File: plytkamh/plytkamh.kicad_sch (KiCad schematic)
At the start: 50 parts, among them J1 USB_C_Receptacle_USB2.0_16P, J2 BOOT0, J3 Conn_01x06, Q1 TEMT6000X01, SW1 RESET, SW2 USER, U1 USBLC6-2SC6, U2 LDL1117S33R, U3 STM32F446RETx, U4 BME280, Y1 12MHz

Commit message: Assign footprints
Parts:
- added J4: COMM, Connector_PinHeader_2.54mm:PinHeader_2x10_P2.54mm_Vertical, symbol Connector_Generic:Conn_02x10_Odd_Even
- added J5: ANALOG_GPIO, Connector_PinHeader_2.54mm:PinHeader_2x10_P2.54mm_Vertical, symbol Connector_Generic:Conn_02x10_Odd_Even
- C1, C10, C11, C12, C13, C14, C15, C16, C17, C18, C2, C3, C4, C5, C6, C7, C8, C9: footprint (none) -> Capacitor_SMD:C_0603_1608Metric
- D2, D3, D4, D5, D6: footprint (none) -> LED_SMD:LED_0603_1608Metric
- F1: footprint (none) -> Fuse:Fuse_1812_4532Metric
- FB1: footprint (none) -> Inductor_SMD:L_0603_1608Metric
- J1: footprint (none) -> Connector_USB:USB_C_Receptacle_GCT_USB4105-xx-A_16P_TopMnt_Horizontal
- J2: footprint (none) -> Connector_PinHeader_2.54mm:PinHeader_1x02_P2.54mm_Vertical
- J3: footprint (none) -> Connector_PinHeader_2.54mm:PinHeader_1x06_P2.54mm_Vertical
- R1, R10, R11, R12, R13, R2, R3, R4, R5, R6, R7, R8, R9: footprint (none) -> Resistor_SMD:R_0603_1608Metric
- SW1, SW2: footprint (none) -> Button_Switch_THT:SW_PUSH_6mm
- U2: footprint LDL1117S33R:SOT230P700X180-4N -> Package_TO_SOT_SMD:SOT-223
- Y1: footprint (none) -> Crystal:Crystal_SMD_3225-4Pin_3.2x2.5mm
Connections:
- net +3.3V: now also J4.1 (Pin_1), J5.1 (Pin_1)
- net +5V: now also J4.2 (Pin_2)
- net GND: now also J4.20 (Pin_20), J4.3 (Pin_3), J4.4 (Pin_4), J5.2 (Pin_2), J5.20 (Pin_20)
- net I2C1_SCL: now also J4.9 (Pin_9)
- net I2C1_SDA: now also J4.10 (Pin_10)
- net PA1: now reaches U3.15 (PA1)
- net PA1: now also J5.9 (Pin_9)
- net USART2_TX: now reaches U3.16 (PA2)
- net USART2_TX: now also J4.5 (Pin_5)
- net USART2_RX: now reaches U3.17 (PA3)
- net USART2_RX: now also J4.6 (Pin_6)
- net PA4: now reaches U3.20 (PA4)
- net PA4: now also J5.10 (Pin_10)
- net PA6: now reaches U3.22 (PA6)
- net PA6: now also J5.13 (Pin_13)
- net PA7: now reaches U3.23 (PA7)
- net PA7: now also J5.14 (Pin_14)
- net PC4: now reaches U3.24 (PC4)
- net PC4: now also J5.7 (Pin_7)
- net PC5: now reaches U3.25 (PC5)
- net PC5: now also J5.8 (Pin_8)
- net PB0: now reaches U3.26 (PB0)
- net PB0: now also J5.11 (Pin_11)
- net PB1: now reaches U3.27 (PB1)
- net PB1: now also J5.12 (Pin_12)
- net I2C2_SCL: now reaches U3.29 (PB10)
- net I2C2_SCL: now also J4.11 (Pin_11)
- net SPI2_NSS: now reaches U3.33 (PB12)
- net SPI2_NSS: now also J4.13 (Pin_13)
- net SPI2_SCK: now reaches U3.34 (PB13)
- net SPI2_SCK: now also J4.14 (Pin_14)
- net SPI2_MISO: now reaches U3.35 (PB14)
- net SPI2_MISO: now also J4.15 (Pin_15)
- net SPI2_MOSI: now reaches U3.36 (PB15)
- net SPI2_MOSI: now also J4.16 (Pin_16)
- net PC9: now reaches U3.40 (PC9)
- net PC9: now also J5.19 (Pin_19)
- net PA8: now reaches U3.41 (PA8)
- net PA8: now also J5.15 (Pin_15)
- net USART1_TX: now reaches U3.42 (PA9)
- net USART1_TX: now also J4.7 (Pin_7)
- net USART1_RX: now reaches U3.43 (PA10)
- net USART1_RX: now also J4.8 (Pin_8)
- net PA15: now reaches U3.50 (PA15)
- net PA15: now also J5.16 (Pin_16)
- net PC10: now reaches U3.51 (PC10)
- net PC10: now also J4.17 (Pin_17)
- net PC11: now reaches U3.52 (PC11)
- net PC11: now also J4.18 (Pin_18)
- net I2C2_SDA: now reaches U3.53 (PC12)
- net I2C2_SDA: now also J4.12 (Pin_12)
- net PB6: now reaches U3.58 (PB6)
- net PB6: now also J5.17 (Pin_17)
- net PB7: now reaches U3.59 (PB7)
- net PB7: now also J5.18 (Pin_18)
- new net: C14.1, U3.6 (PH1), Y1.3
- new net PC0: J5.3 (Pin_3), U3.8 (PC0)
- new net PC1: J5.4 (Pin_4), U3.9 (PC1)
- new net PC2: J5.5 (Pin_5), U3.10 (PC2)
- new net PC3: J5.6 (Pin_6), U3.11 (PC3)
- new net PD2: J4.19 (Pin_19), U3.54 (PD2)
- no-connect marks 2 -> 6
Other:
- moved on the sheet: C10, C11, C12, C13, C14, C15, C16, C17, C18, C4, C5, C6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

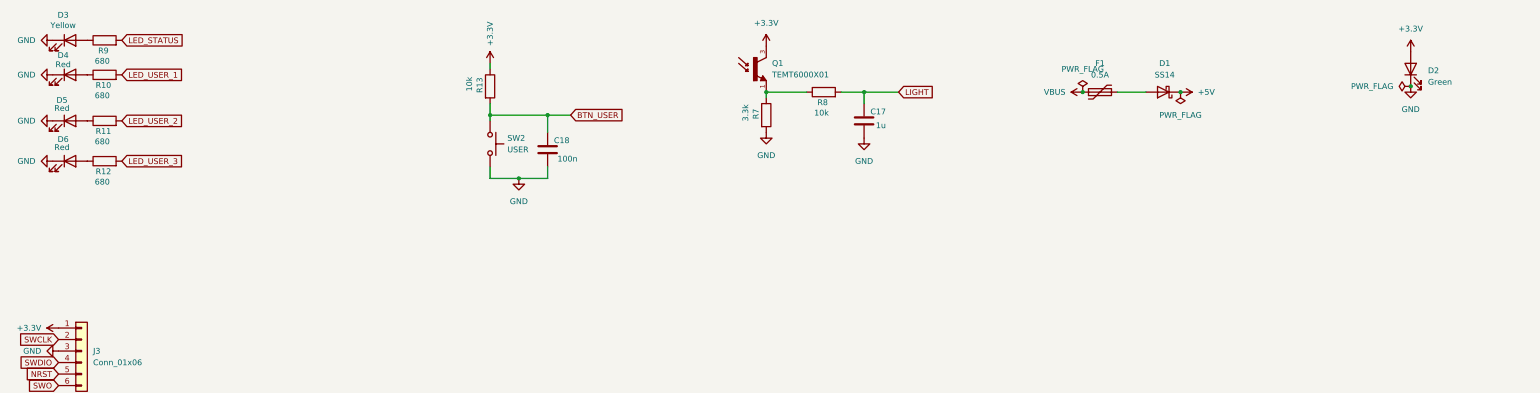
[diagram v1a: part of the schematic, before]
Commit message: component placement
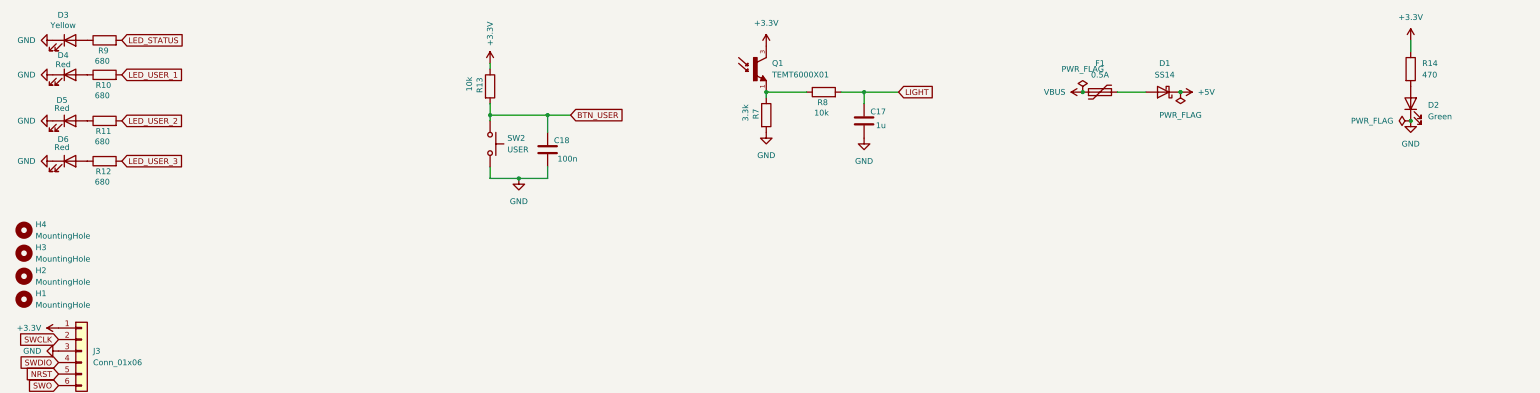
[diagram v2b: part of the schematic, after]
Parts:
- added H1, H2, H3, H4: MountingHole, MountingHole:MountingHole_3.2mm_M3, symbol Mechanical:MountingHole
- added R14: 470, Resistor_SMD:R_0603_1608Metric, symbol Device:R
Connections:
- net +3.3V: now also R14.1; no longer D2.2 (A)
- new net: D2.2 (A), R14.2
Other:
- moved on the sheet: D2

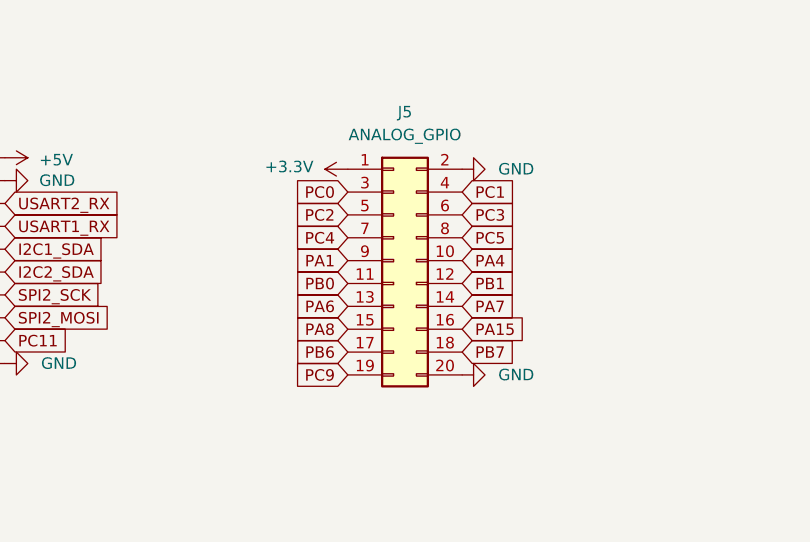
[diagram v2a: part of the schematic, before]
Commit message: J5 pin swap
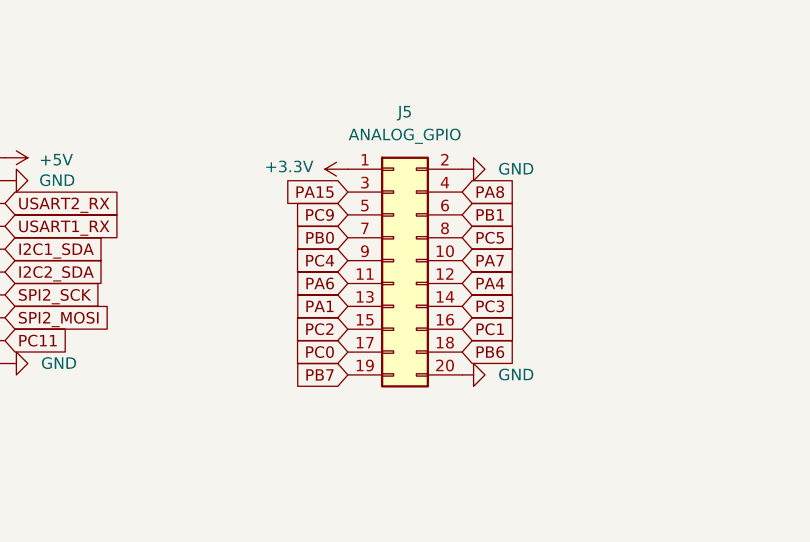
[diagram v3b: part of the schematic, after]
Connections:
- net PA1: now also J5.13 (Pin_13); no longer J5.9 (Pin_9)
- net PA15: now also J5.3 (Pin_3); no longer J5.16 (Pin_16)
- net PA4: now also J5.12 (Pin_12); no longer J5.10 (Pin_10)
- net PA6: now also J5.11 (Pin_11); no longer J5.13 (Pin_13)
- net PA7: now also J5.10 (Pin_10); no longer J5.14 (Pin_14)
- net PA8: now also J5.4 (Pin_4); no longer J5.15 (Pin_15)
- net PB0: now also J5.7 (Pin_7); no longer J5.11 (Pin_11)
- net PB1: now also J5.6 (Pin_6); no longer J5.12 (Pin_12)
- net PB6: now also J5.18 (Pin_18); no longer J5.17 (Pin_17)
- net PB7: now also J5.19 (Pin_19); no longer J5.18 (Pin_18)
- net PC0: now also J5.17 (Pin_17); no longer J5.3 (Pin_3)
- net PC1: now also J5.16 (Pin_16); no longer J5.4 (Pin_4)
- net PC2: now also J5.15 (Pin_15); no longer J5.5 (Pin_5)
- net PC3: now also J5.14 (Pin_14); no longer J5.6 (Pin_6)
- net PC4: now also J5.9 (Pin_9); no longer J5.7 (Pin_7)
- net PC9: now also J5.5 (Pin_5); no longer J5.19 (Pin_19)

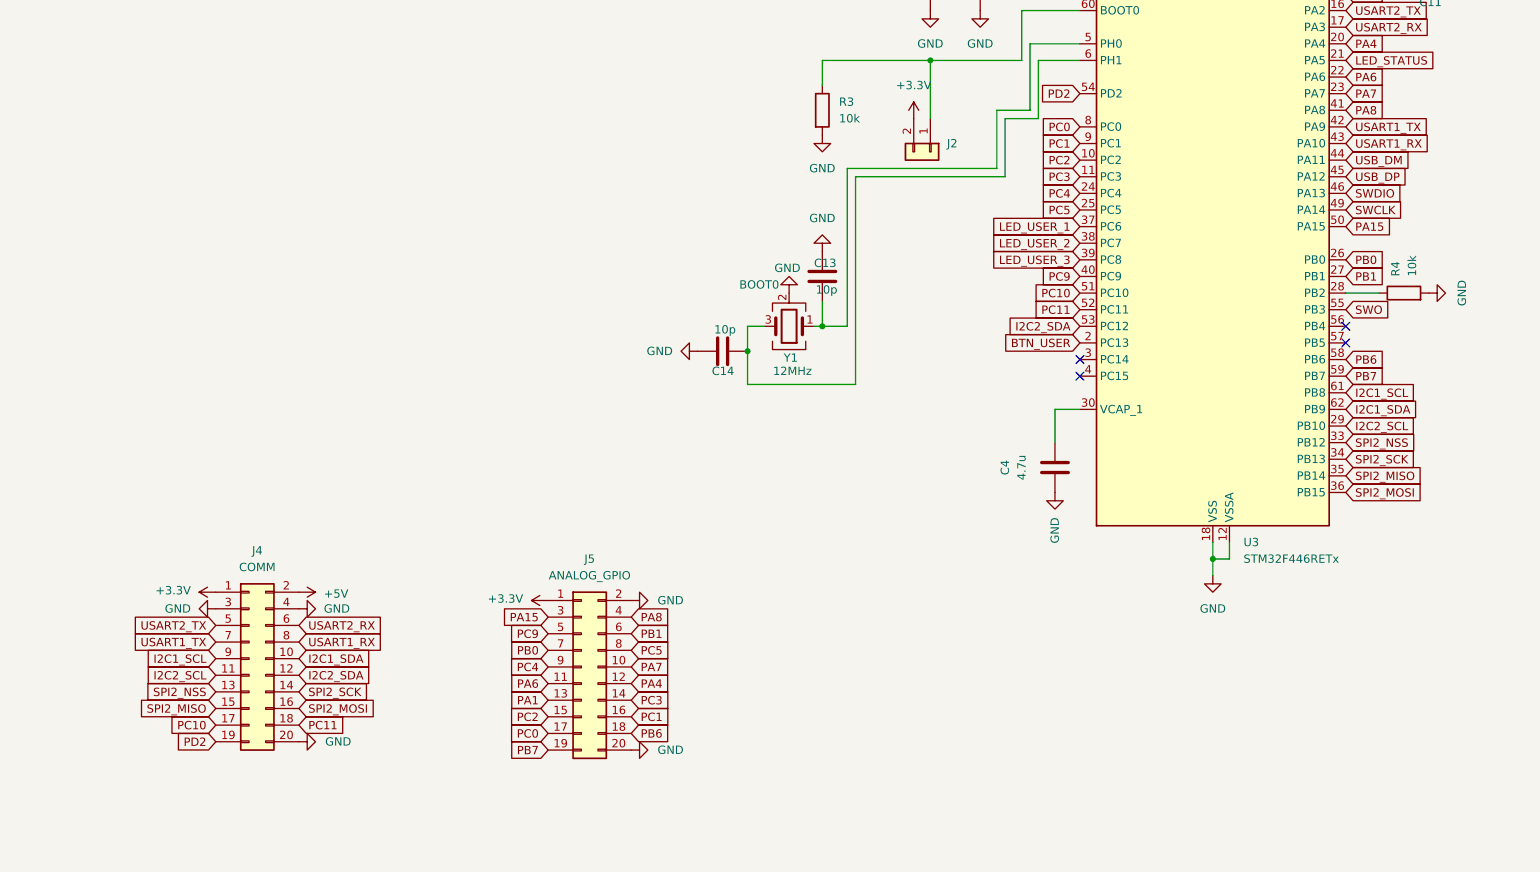
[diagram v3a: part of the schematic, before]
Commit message: Remaped headers, routed the mcu and j4,j5, almost finished
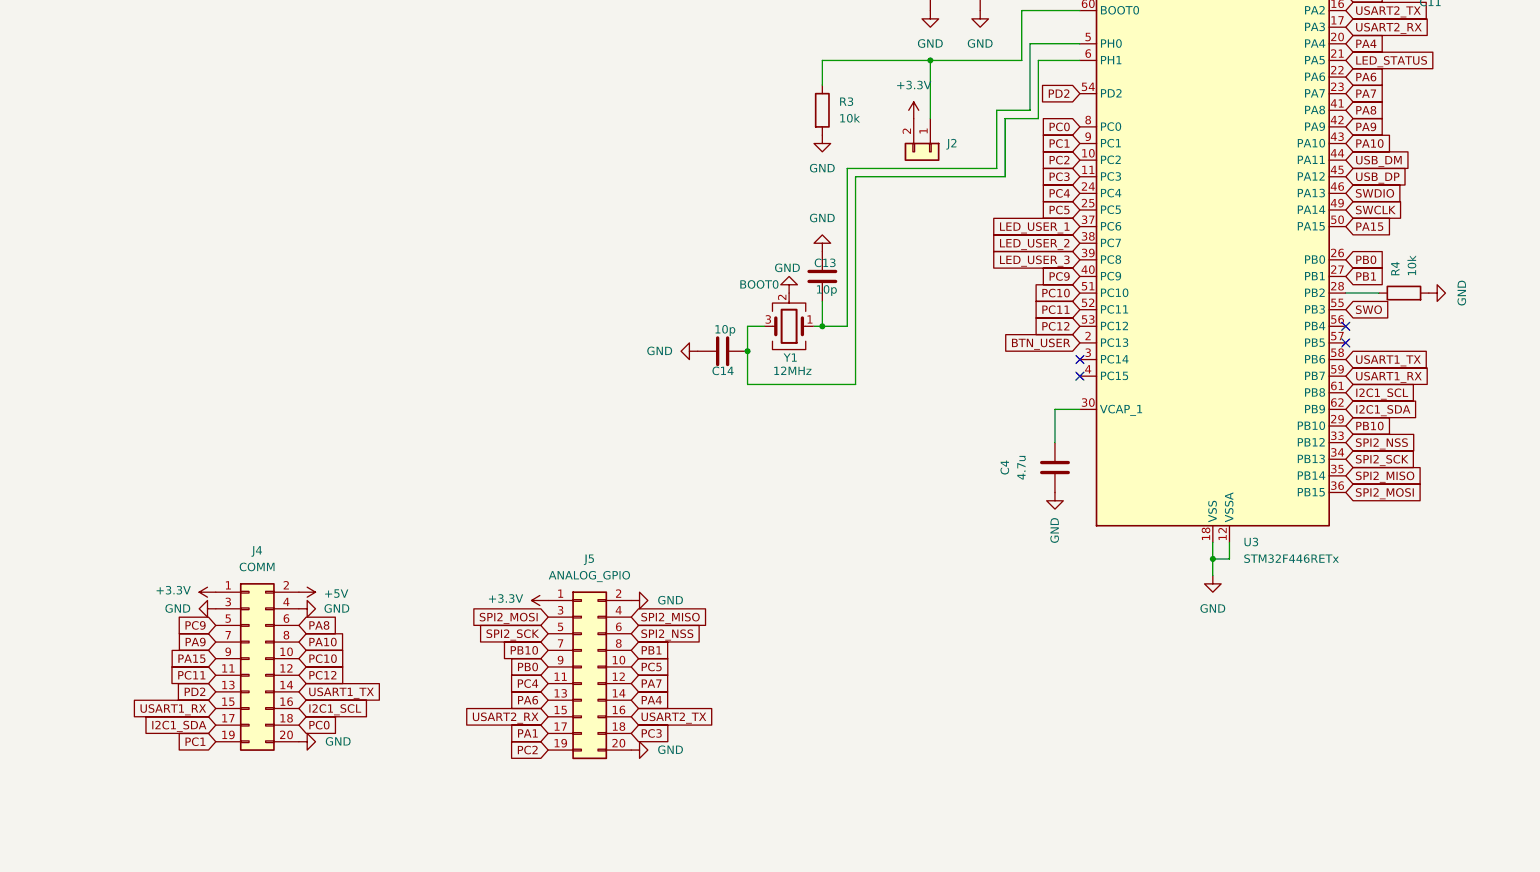
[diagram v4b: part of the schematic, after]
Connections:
- net I2C1_SCL: now also J4.16 (Pin_16); no longer J4.9 (Pin_9)
- net I2C1_SDA: now also J4.17 (Pin_17); no longer J4.10 (Pin_10)
- net PA1: now also J5.17 (Pin_17); no longer J5.13 (Pin_13)
- net PA15: now also J4.9 (Pin_9); no longer J5.3 (Pin_3)
- net PA4: now also J5.14 (Pin_14); no longer J5.12 (Pin_12)
- net PA6: now also J5.13 (Pin_13); no longer J5.11 (Pin_11)
- net PA7: now also J5.12 (Pin_12); no longer J5.10 (Pin_10)
- net PA8: now also J4.6 (Pin_6); no longer J5.4 (Pin_4)
- net PB0: now also J5.9 (Pin_9); no longer J5.7 (Pin_7)
- net PB1: now also J5.8 (Pin_8); no longer J5.6 (Pin_6)
- net PC0: now also J4.18 (Pin_18); no longer J5.17 (Pin_17)
- net PC1: now also J4.19 (Pin_19); no longer J5.16 (Pin_16)
- net PC10: now also J4.10 (Pin_10); no longer J4.17 (Pin_17)
- net PC11: now also J4.11 (Pin_11); no longer J4.18 (Pin_18)
- net PC2: now also J5.19 (Pin_19); no longer J5.15 (Pin_15)
- net PC3: now also J5.18 (Pin_18); no longer J5.14 (Pin_14)
- net PC4: now also J5.11 (Pin_11); no longer J5.9 (Pin_9)
- net PC5: now also J5.10 (Pin_10); no longer J5.8 (Pin_8)
- net PC9: now also J4.5 (Pin_5); no longer J5.5 (Pin_5)
- net PD2: now also J4.13 (Pin_13); no longer J4.19 (Pin_19)
- net SPI2_MISO: now also J5.4 (Pin_4); no longer J4.15 (Pin_15)
- net SPI2_MOSI: now also J5.3 (Pin_3); no longer J4.16 (Pin_16)
- net SPI2_NSS: now also J5.6 (Pin_6); no longer J4.13 (Pin_13)
- net SPI2_SCK: now also J5.5 (Pin_5); no longer J4.14 (Pin_14)
- net USART1_RX: now also J4.15 (Pin_15), U3.59 (PB7); no longer J4.8 (Pin_8), U3.43 (PA10)
- net USART1_TX: now also J4.14 (Pin_14), U3.58 (PB6); no longer J4.7 (Pin_7), U3.42 (PA9)
- net USART2_RX: now also J5.15 (Pin_15); no longer J4.6 (Pin_6)
- net USART2_TX: now also J5.16 (Pin_16); no longer J4.5 (Pin_5)
- net I2C2_SCL renamed PB10
- net PB10: now also J5.7 (Pin_7); no longer J4.11 (Pin_11)
- net I2C2_SDA renamed PC12
- removed net PB6: J5.18 (Pin_18), U3.58 (PB6)
- removed net PB7: J5.19 (Pin_19), U3.59 (PB7)
- new net PA10: J4.8 (Pin_8), U3.43 (PA10)
- new net PA9: J4.7 (Pin_7), U3.42 (PA9)

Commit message: docs: readme, pictures, schematic sections
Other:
- note added: "CONNECTORS"
- note added: "MECHANICAL"
- note added: "MICROCONTROLLER"
- note added: "POWER SUPPLY"
- note added: "SENSORS"
- note added: "USER INTERFACE"
- moved on the sheet: C1, C10, C11, C12, C13, C14, C15, C16, C17, C18, C2, C3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
